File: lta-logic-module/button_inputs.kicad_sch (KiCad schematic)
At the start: 26 parts

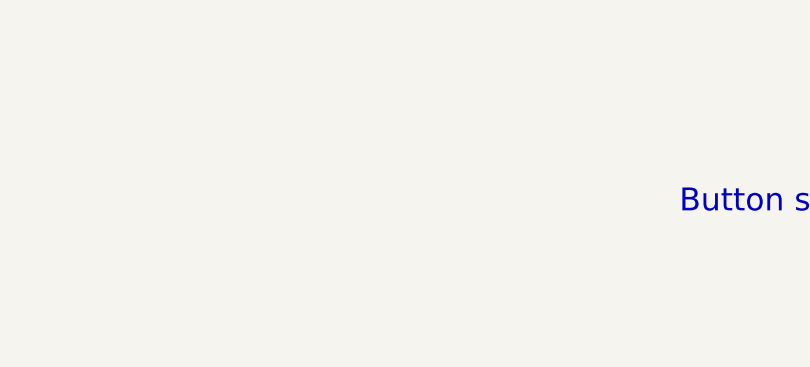
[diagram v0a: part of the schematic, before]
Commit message: Add test points
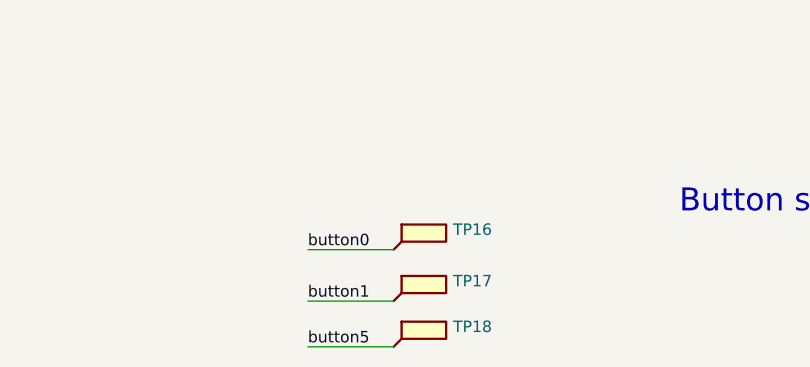
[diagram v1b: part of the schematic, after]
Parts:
- added TP16, TP17, TP18: (no value), symbol Connector:TestPoint_Flag
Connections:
- net button0: now also TP16.1
- net button1: now also TP17.1
- net button5: now also TP18.1
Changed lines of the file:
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@@
+    (stroke (width 0) (type default) (color 0 0 0 0))
+  )
+  (wire (pts (xy 144.78 179.07) (xy 154.305 179.07))
     (stroke (width 0) (type default) (color 0 0 0 0))
   )
@@
     (stroke (width 0) (type default) (color 0 0 0 0))
   )
+  (wire (pts (xy 144.78 184.785) (xy 154.305 184.785))
+    (stroke (width 0) (type default) (color 0 0 0 0))
+  )
   (wire (pts (xy 99.06 96.52) (xy 134.62 96.52))
     (stroke (width 0) (type default) (color 0 0 0 0))
@@
   )
   (wire (pts (xy 31.75 81.915) (xy 53.975 81.915))
+    (stroke (width 0) (type default) (color 0 0 0 0))
+  )
+  (wire (pts (xy 144.78 189.865) (xy 154.305 189.865))
     (stroke (width 0) (type default) (color 0 0 0 0))
   )
@@
     (effects (font (size 1.27 1.27)) (justify right bottom))
   )
+  (label "button1" (at 144.78 184.785 0)
+    (effects (font (size 1.27 1.27)) (justify left bottom))
+  )
   (label "button4" (at 163.83 71.755 0)
     (effects (font (size 1.27 1.27)) (justify left bottom))
@@
     (effects (font (size 1.27 1.27)) (justify left bottom))
   )
+  (label "button5" (at 144.78 189.865 0)
+    (effects (font (size 1.27 1.27)) (justify left bottom))
+  )
   (label "btn_buf3" (at 128.27 69.215 0)
     (effects (font (size 1.27 1.27)) (justify left bottom))
@@
   (label "btn_in8" (at 40.005 94.615 180)
     (effects (font (size 1.27 1.27)) (justify right bottom))
+  )
+  (label "button0" (at 144.78 179.07 0)
+    (effects (font (size 1.27 1.27)) (justify left bottom))
   )
   (label "btn_buf7" (at 128.27 101.6 0)
@@
     )
     (property "Datasheet" "" (id 3) (at 36.83 99.695 0)
+      (effects (font (size 1.27 1.27)) hide)
+    )
+    (pin "1")
+  )
+  (symbol (lib_id "Connector:TestPoint_Flag") (at 154.305 189.865 0) (unit 1)
+    (in_bom no) (on_board yes) (fields_autoplaced)
+    (property "Reference" "TP18" (id 0) (at 160.909 187.6333 0)
+      (effects (font (size 1.27 1.27)) (justify left))
+    )
+    (property "Value" "" (id 1) (at 160.909 190.1702 0)
+      (effects (font (size 1.27 1.27)) (justify left))
+    )
+    (property "Footprint" "" (id 2) (at 159.385 189.865 0)
+      (effects (font (size 1.27 1.27)) hide)
+    )
+    (property "Datasheet" "~" (id 3) (at 159.385 189.865 0)
       (effects (font (size 1.27 1.27)) hide)
     )
@@
     (pin "2")
   )
+  (symbol (lib_id "Connector:TestPoint_Flag") (at 154.305 179.07 0) (unit 1)
+    (in_bom no) (on_board yes) (fields_autoplaced)
+    (property "Reference" "TP16" (id 0) (at 160.909 176.8383 0)
+      (effects (font (size 1.27 1.27)) (justify left))
+    )
+    (property "Value" "" (id 1) (at 160.909 179.3752 0)
+      (effects (font (size 1.27 1.27)) (justify left))
+    )
+    (property "Footprint" "" (id 2) (at 159.385 179.07 0)
+      (effects (font (size 1.27 1.27)) hide)
+    )
+    (property "Datasheet" "~" (id 3) (at 159.385 179.07 0)
+      (effects (font (size 1.27 1.27)) hide)
+    )
+    (pin "1")
+  )
   (symbol (lib_id "Device:R_Small") (at 74.295 109.22 0) (unit 1)
     (in_bom yes) (on_board yes) (fields_autoplaced)
@@
     (pin "2")
   )
+  (symbol (lib_id "Connector:TestPoint_Flag") (at 154.305 184.785 0) (unit 1)
+    (in_bom no) (on_board yes) (fields_autoplaced)
+    (property "Reference" "TP17" (id 0) (at 160.909 182.5533 0)
+      (effects (font (size 1.27 1.27)) (justify left))
+    )
+    (property "Value" "" (id 1) (at 160.909 185.0902 0)
+      (effects (font (size 1.27 1.27)) (justify left))
+    )
+    (property "Footprint" "" (id 2) (at 159.385 184.785 0)
+      (effects (font (size 1.27 1.27)) hide)
+    )
+    (property "Datasheet" "~" (id 3) (at 159.385 184.785 0)
+      (effects (font (size 1.27 1.27)) hide)
+    )
+    (pin "1")
+  )
   (symbol (lib_id "Device:R_Small") (at 110.49 66.675 90) (unit 1)

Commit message: Fix GND path return.
* Route power traces over ground plane.
* Add routed corners to edge cuts
* Remove final TODO notes.
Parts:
- J2: Comment (none) -> Molex Micro-Latch 12-pin
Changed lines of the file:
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@@
       (effects (font (size 1.524 1.524)) hide)
     )
-    (property "Comment" "" (id 4) (at 31.75 69.215 0)
+    (property "Comment" "Molex Micro-Latch 12-pin" (id 4) (at 31.75 69.215 0)
       (effects (font (size 1.27 1.27)) hide)
     )

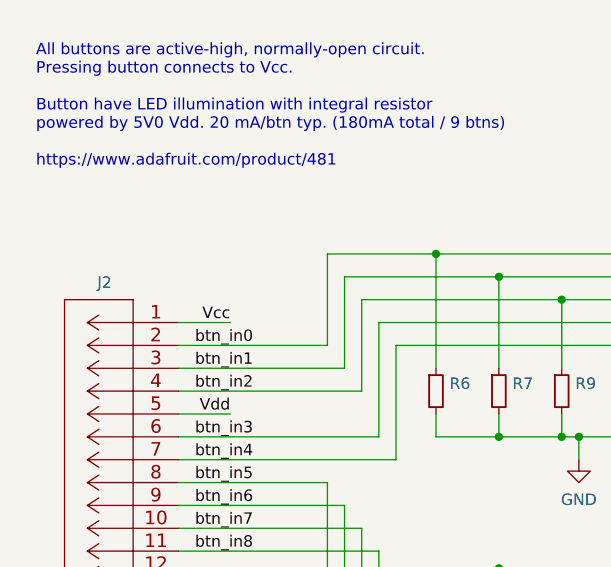
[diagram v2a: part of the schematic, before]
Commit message: Add indicator LED to SW1 enabled.
Adds 220K pull-down resistor to DARK signal. (Validated.)
Update solder thief pads and process direction indicator.
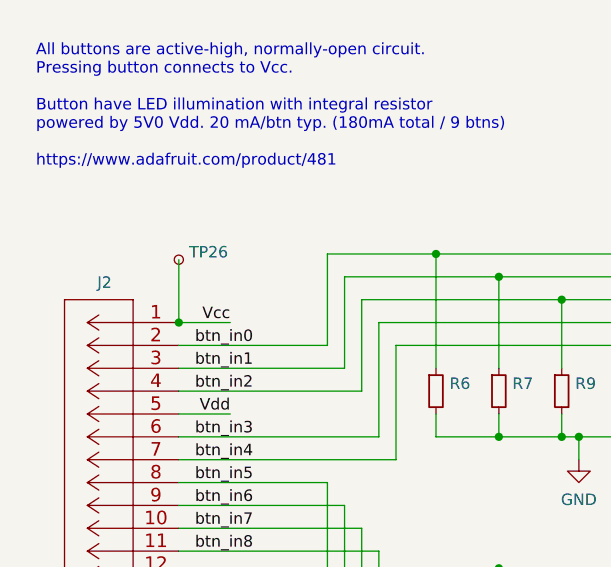
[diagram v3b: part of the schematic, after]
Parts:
- added TP26: (no value), symbol Connector:TestPoint_Small
- J2: Comment Molex Micro-Latch 12-pin -> Molex Micro-Latch, 12-pin
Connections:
- net Vcc: now also TP26.1
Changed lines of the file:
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@@
   (junction (at 88.265 71.755) (diameter 0) (color 0 0 0 0)
+  )
+  (junction (at 31.75 69.215) (diameter 0) (color 0 0 0 0)
   )
   (junction (at 60.325 61.595) (diameter 0) (color 0 0 0 0)
@@
     (stroke (width 0) (type default) (color 0 0 0 0))
   )
+  (wire (pts (xy 31.75 62.23) (xy 31.75 69.215))
+    (stroke (width 0) (type default) (color 0 0 0 0))
+  )
   (wire (pts (xy 31.75 92.075) (xy 52.07 92.075))
     (stroke (width 0) (type default) (color 0 0 0 0))
@@
     (pin "1")
     (pin "2")
+  )
+  (symbol (lib_id "Connector:TestPoint_Small") (at 31.75 62.23 0) (unit 1)
+    (in_bom no) (on_board yes)
+    (property "Reference" "TP26" (id 0) (at 32.893 61.3953 0)
+      (effects (font (size 1.27 1.27)) (justify left))
+    )
+    (property "Value" "" (id 1) (at 32.893 63.9322 0)
+      (effects (font (size 1.27 1.27)) (justify left))
+    )
+    (property "Footprint" "" (id 2) (at 36.83 62.23 0)
+      (effects (font (size 1.27 1.27)) hide)
+    )
+    (property "Datasheet" "~" (id 3) (at 36.83 62.23 0)
+      (effects (font (size 1.27 1.27)) hide)
+    )
+    (pin "1")
   )
   (symbol (lib_id "Device:R_Small") (at 118.11 104.14 90) (unit 1)
@@
       (effects (font (size 1.524 1.524)) hide)
     )
-    (property "Comment" "Molex Micro-Latch 12-pin" (id 4) (at 31.75 69.215 0)
-      (effects (font (size 1.27 1.27)) hide)
-    )
+    (property "Comment" "Molex Micro-Latch, 12-pin" (id 4) (at 31.75 69.215 0)
+      (effects (font (size 1.27 1.27)) hide)
+    )

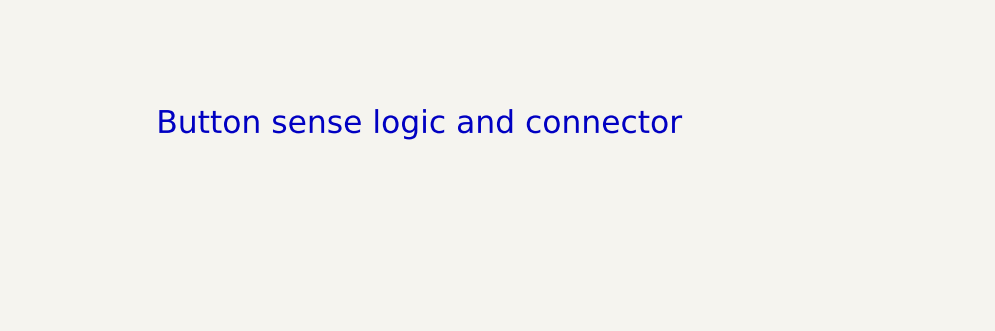
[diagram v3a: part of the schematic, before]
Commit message: Generate logic module 2022-05-08 v1.0 fab documentation.
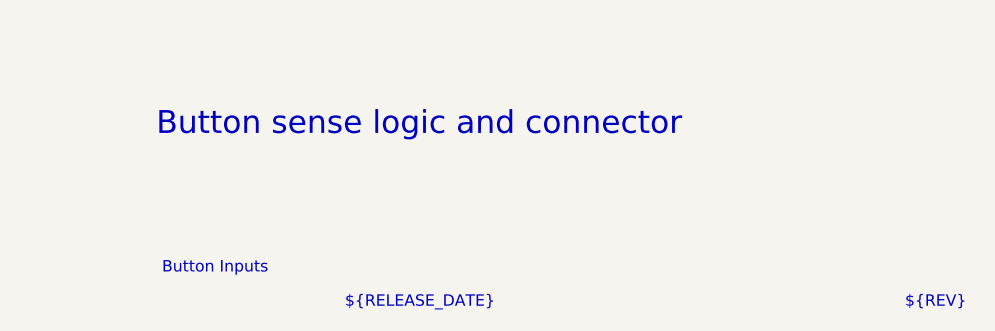
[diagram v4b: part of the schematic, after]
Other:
- note added: "${RELEASE_DATE}"
- note added: "${REV}"
- note added: "Button Inputs"
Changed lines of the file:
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@@
+    (effects (font (size 1.27 1.27)) (justify left bottom))
+  )
+  (text "${REV}" (at 269.24 194.31 0)
     (effects (font (size 1.27 1.27)) (justify left bottom))
   )
   (text "Button sense logic and connector" (at 186.055 175.26 0)
     (effects (font (size 2.54 2.54)) (justify left bottom))
+  )
+  (text "${RELEASE_DATE}" (at 207.01 194.31 0)
+    (effects (font (size 1.27 1.27)) (justify left bottom))
   )
   (text "3V3 logic through buttons" (at 29.845 17.78 0)
@@
     (effects (font (size 1.27 1.27)) (justify left bottom))
   )
+  (text "Button Inputs" (at 186.69 190.5 0)
+    (effects (font (size 1.27 1.27)) (justify left bottom))
+  )

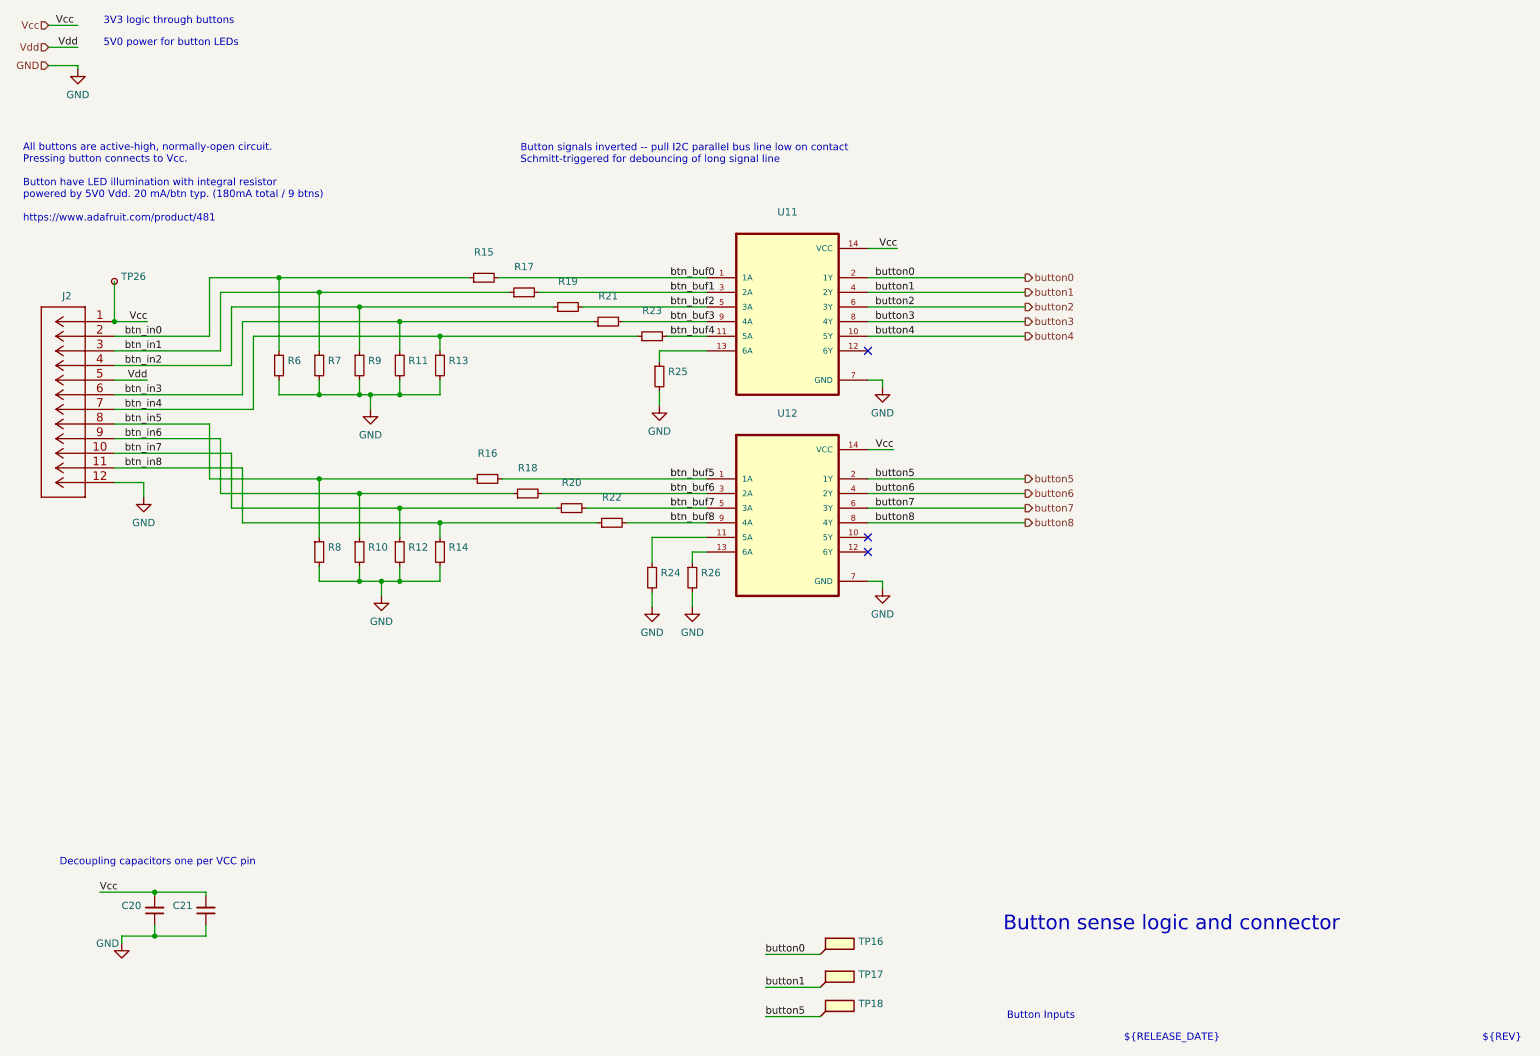
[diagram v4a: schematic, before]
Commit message: Update logic module power budget from button LED measurements.
Button LEDs draw ~11mA each (98 mA total) empirically; not the ~20mA each
I initially guessed for estimating purposes.
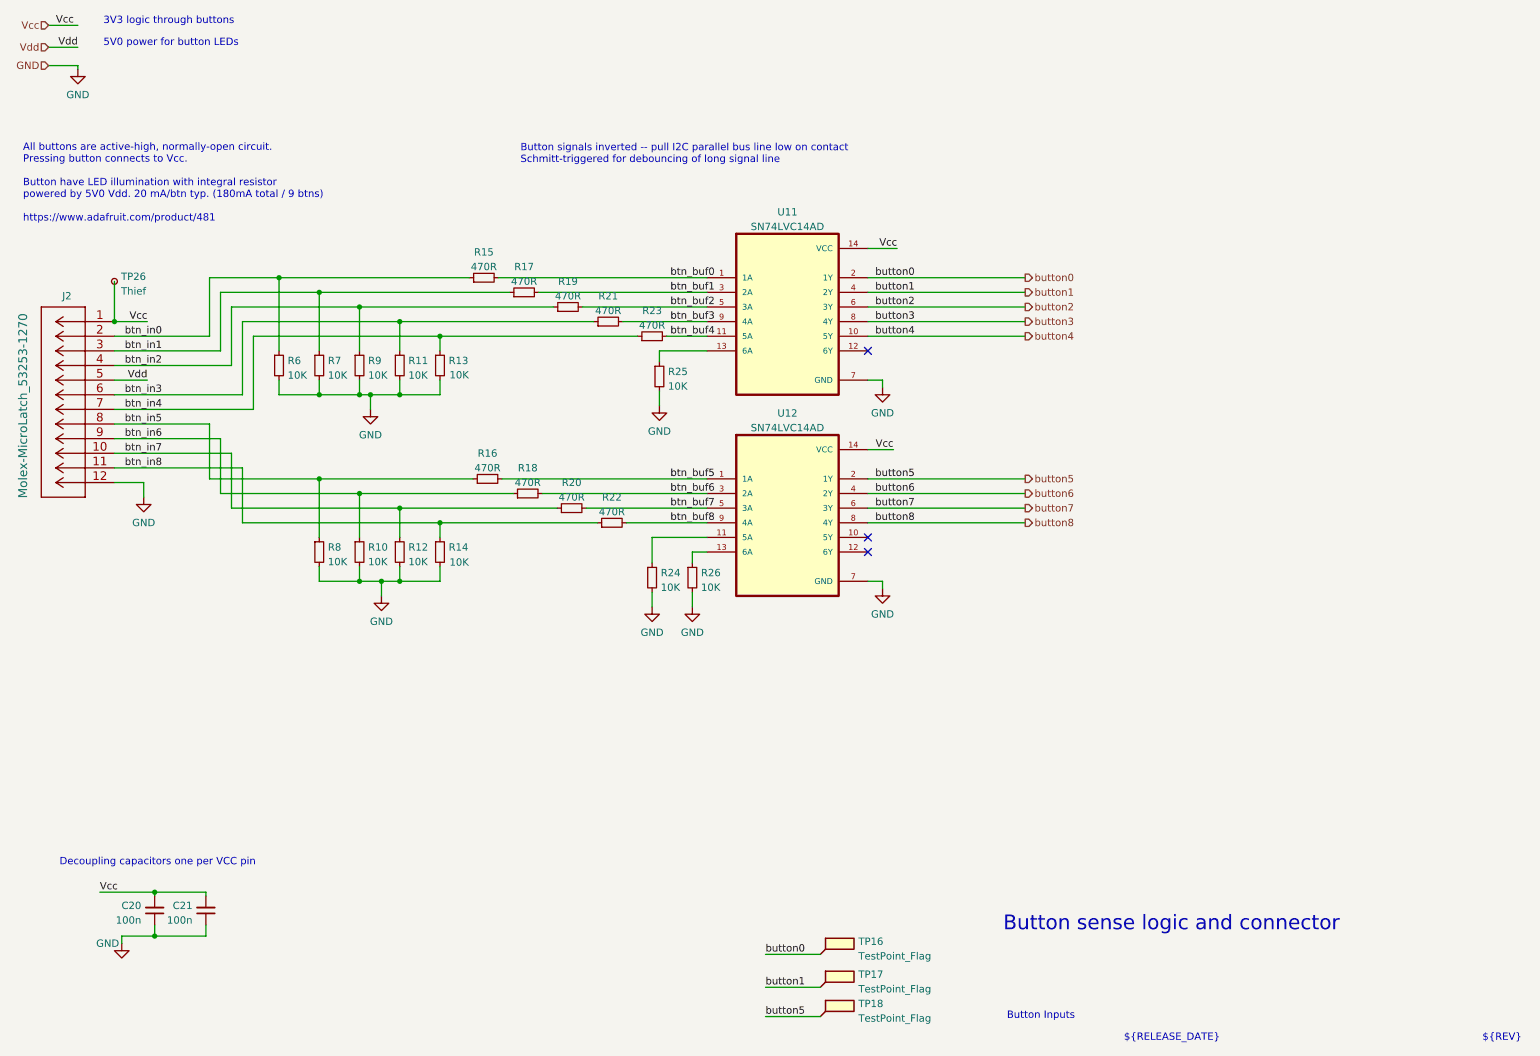
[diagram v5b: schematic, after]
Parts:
- C20, C21: value (none) -> 100n; footprint (none) -> Capacitor_SMD:C_0603_1608Metric
- J2: value (none) -> Molex-MicroLatch_53253-1270; footprint (none) -> Aaron_THT:Molex-MicroLatch-53253-1270
- R10, R11, R12, R13, R14, R24, R25, R26, R6, R7, R8, R9: value (none) -> 10K; footprint (none) -> Resistor_SMD:R_0603_1608Metric
- R15, R16, R17, R18, R19, R20, R21, R22, R23: value (none) -> 470R; footprint (none) -> Resistor_SMD:R_0603_1608Metric
- TP16, TP17, TP18: value (none) -> TestPoint_Flag; footprint (none) -> Aaron_THT:TestPoint_THTPad_1.0x1.0mm_Drill0.3mm
- TP26: value (none) -> Thief; footprint (none) -> Aaron_Pads:Pad_1.5x1.5mm
- U11, U12: value (none) -> SN74LVC14AD; footprint (none) -> Aaron_TI_Parts:TI_SOIC_D_R-PDSO-G14
